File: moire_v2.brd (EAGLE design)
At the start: 39.4 x 100 mm, 141 parts, among them IC1 R-78E3.3-0.5, IC14 TL074PW, IC2 LD2981, IC3 LM4040B25, IC4 4051PW, IC5 TLC59281DBQ, IC6 LM324PW, J1 PJ301_THONKICONN6, J10 PJ301_THONKICONN6, J11 PJ301_THONKICONN6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

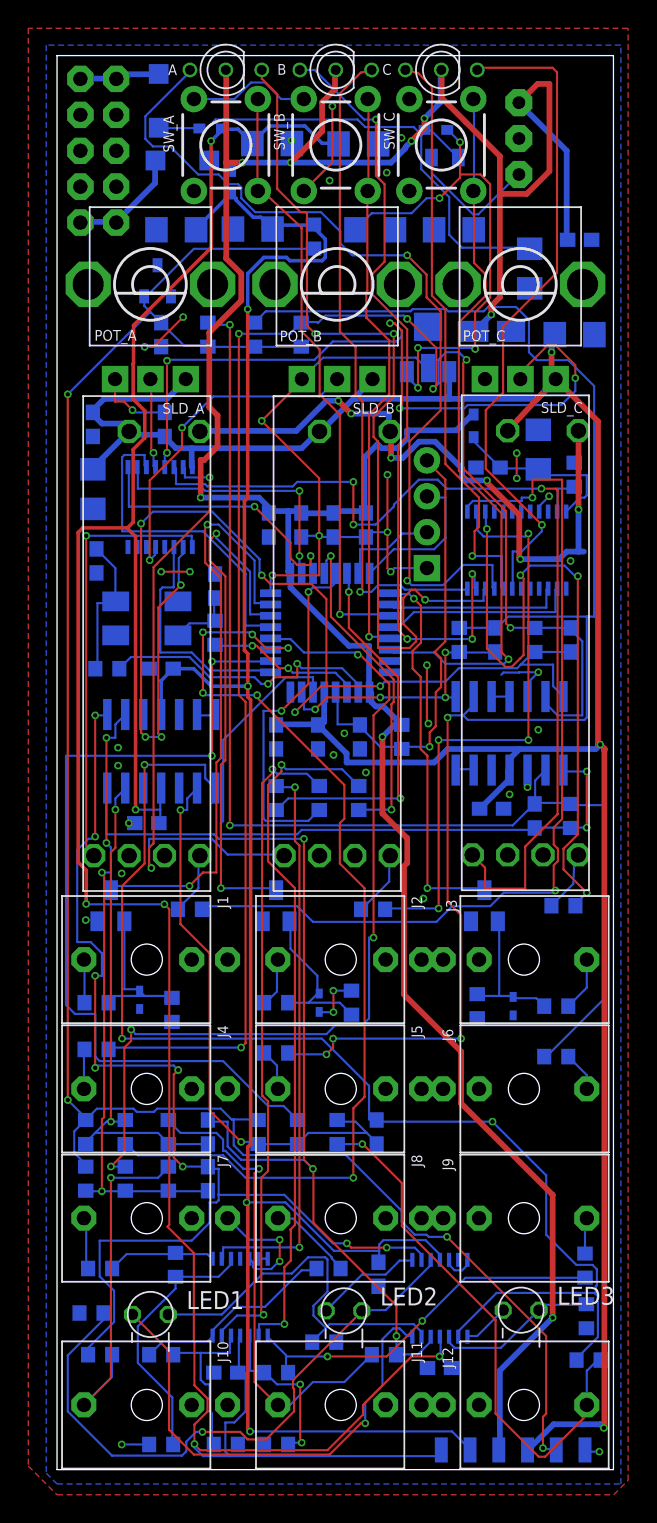
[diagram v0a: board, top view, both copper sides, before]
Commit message: align C slider
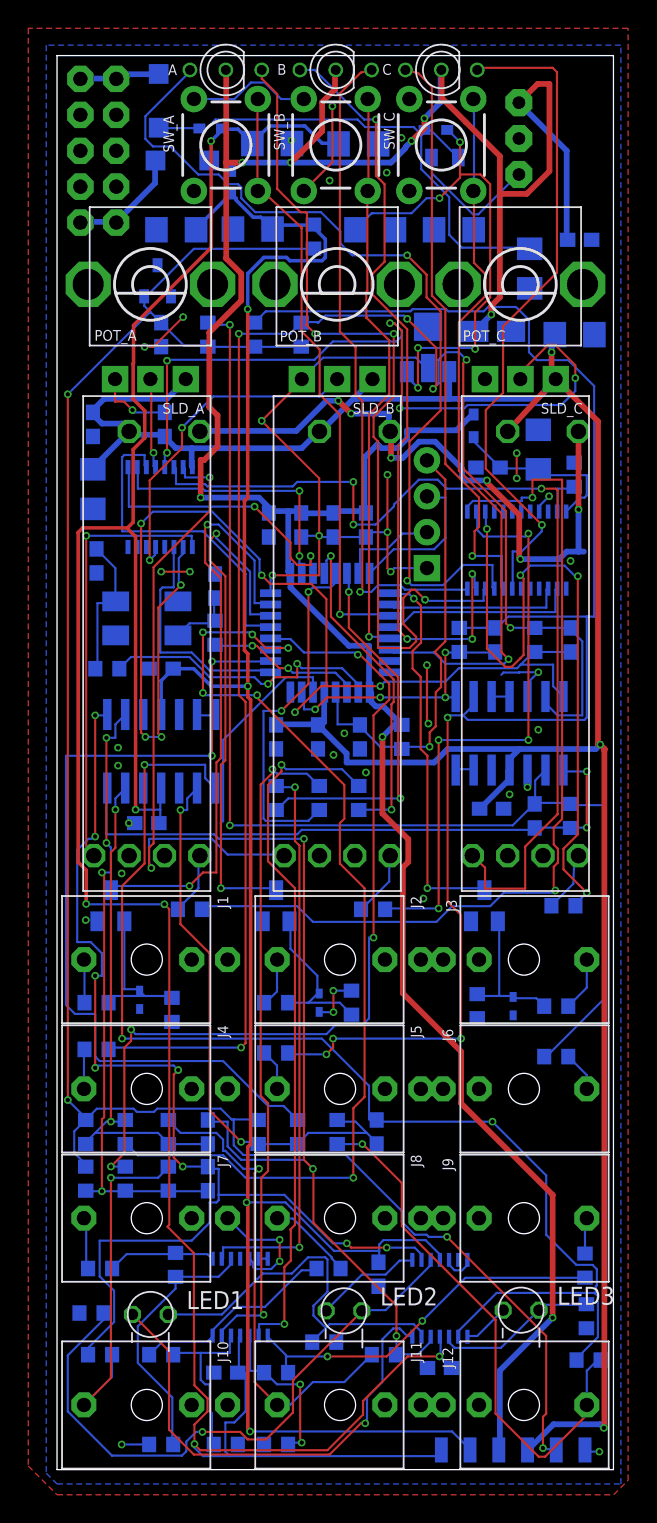
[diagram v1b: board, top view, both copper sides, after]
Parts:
- moved J11 0.05 mm to (20.0, 4.57)
- moved J2 0.05 mm to (20.0, 36.1)
- moved J5 0.05 mm to (20.0, 26.9)
- moved J8 0.05 mm to (20.0, 17.8)
- moved SLD_C 0.05 mm to (33.1, 58.4)
